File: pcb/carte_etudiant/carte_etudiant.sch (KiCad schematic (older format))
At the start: 3 parts, among them J1 Conn_02x15_Odd_Even, J2 Conn_01x14, U1 NUCLEO64-F103RB

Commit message: * Passage d un connecteur 30 pts à un connecteur 40 pts sur la carte etudiant * Correction sur le fichier de pinout (changement du nom du signal SERVO_PWM en SERVO_VOILE_PWM)
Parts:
- J1: footprint Insa:TE 5530841-2 PCB Edge -> Insa:5-5530843-4-PCB; symbol Connector_Generic:Conn_02x15_Odd_Even -> Connector_Generic:Conn_02x20_Odd_Even
- J2: footprint Connector_PinHeader_2.54mm:PinHeader_1x14_P2.54mm_Vertical -> Connector_PinHeader_2.54mm:PinHeader_1x16_P2.54mm_Vertical; symbol Connector_Generic:Conn_01x14 -> Connector_Generic:Conn_01x16
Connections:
- net labels added: +5V, CAPTEUR_I2C_SCL, CAPTEUR_I2C_SDA, CAPTEUR_SPI_CLK, CAPTEUR_SPI_CS, CAPTEUR_SPI_MISO, CAPTEUR_SPI_MOSI, GIROUETTE_INDEX, GIROUETTE_PHA, GIROUETTE_PHB, PLATEAU_DIRECTION, PLATEAU_PWM, SERVO_VOILE_PWM, TENSION_BATTERIE, XBEE_UART_RX, XBEE_UART_TX
- net labels removed: +3V3
- wire segments 49 -> 65
- no-connect marks 79 -> 83
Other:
- note removed: "Girouette Index"
- note removed: "Girouette PH-A"
- note removed: "Girouette PH-B"
- note removed: "I2C SCL"
- note removed: "I2C SDA"
- note removed: "Moteur Direction"
- note removed: "Moteur PWM"
- note removed: "Servo PWM"
- note removed: "Tension Batterie"
- note removed: "XBEE RX"
- note removed: "XBEE TX"

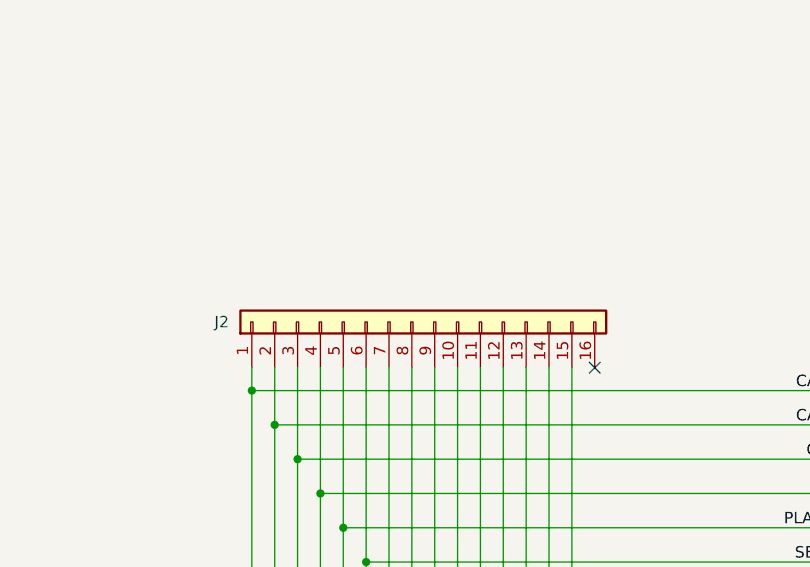
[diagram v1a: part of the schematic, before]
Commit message: modif sur la carte etudiant (changement de coté)
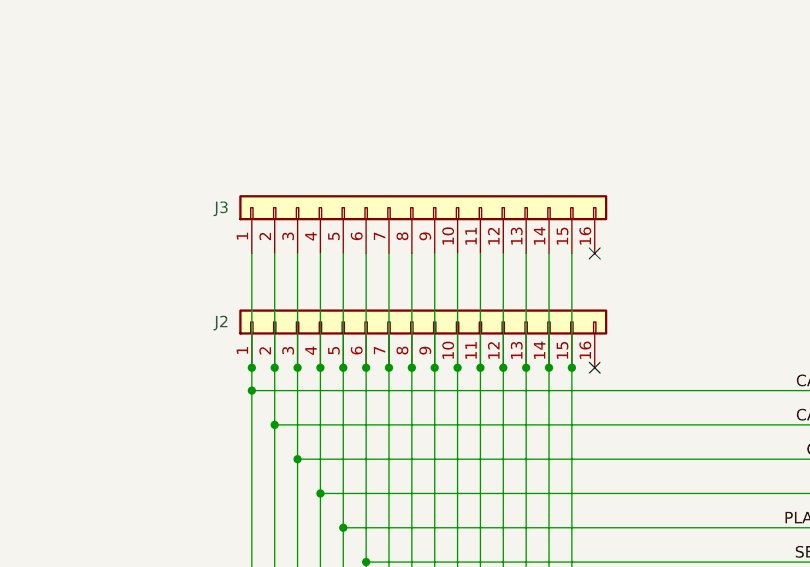
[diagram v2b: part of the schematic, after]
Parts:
- added J3: Conn_01x14, Connector_PinSocket_2.54mm:PinSocket_1x16_P2.54mm_Vertical, symbol Connector_Generic:Conn_01x16
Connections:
- wire segments 65 -> 80
- no-connect marks 83 -> 84
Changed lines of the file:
@@
 	6350 4750 6250 4750
 $Comp
-L power:GND #PWR?
+L power:GND #PWR0101
 U 1 1 5E4A3E36
 P 6250 4750
-F 0 "#PWR?" H 6250 4500 50  0001 C CNN
+F 0 "#PWR0101" H 6250 4500 50  0001 C CNN
 F 1 "GND" H 6255 4577 50  0000 C CNN
 F 2 "" H 6250 4750 50  0001 C CNN
@@
 $EndComp
 $Comp
-L power:GND #PWR?
+L power:GND #PWR0103
 U 1 1 5E4A485B
 P 3700 5350
-F 0 "#PWR?" H 3700 5100 50  0001 C CNN
+F 0 "#PWR0103" H 3700 5100 50  0001 C CNN
 F 1 "GND" H 3705 5177 50  0000 C CNN
 F 2 "" H 3700 5350 50  0001 C CNN
@@
 	3800 1250 3800 950
 $Comp
-L power:+5V #PWR?
+L power:+5V #PWR0104
 U 1 1 5E77E45F
 P 3800 950
-F 0 "#PWR?" H 3800 800 50  0001 C CNN
+F 0 "#PWR0104" H 3800 800 50  0001 C CNN
 F 1 "+5V" H 3815 1123 50  0000 C CNN
 F 2 "" H 3800 950 50  0001 C CNN
@@
 $EndComp
 $Comp
-L power:+5V #PWR?
+L power:+5V #PWR0105
 U 1 1 5E77F67D
 P 10750 1050
-F 0 "#PWR?" H 10750 900 50  0001 C CNN
+F 0 "#PWR0105" H 10750 900 50  0001 C CNN
 F 1 "+5V" H 10765 1223 50  0000 C CNN
 F 2 "" H 10750 1050 50  0001 C CNN
@@
 $EndComp
 $Comp
-L power:+5V #PWR?
+L power:+5V #PWR0106
 U 1 1 5E780E0F
 P 6550 5050
-F 0 "#PWR?" H 6550 4900 50  0001 C CNN
+F 0 "#PWR0106" H 6550 4900 50  0001 C CNN
 F 1 "+5V" H 6565 5223 50  0000 C CNN
 F 2 "" H 6550 5050 50  0001 C CNN
@@
 	1    0    0    -1
 $EndComp
+$Comp
+L Connector_Generic:Conn_01x16 J3
+U 1 1 60081935
+P 7350 1950
+F 0 "J3" V 7350 2750 50  0000 L CNN
+F 1 "Conn_01x14" H 7430 1851 50  0001 L CNN
+F 2 "Connector_PinSocket_2.54mm:PinSocket_1x16_P2.54mm_Vertical" H 7350 1950 50  0001 C CNN
+F 3 "~" H 7350 1950 50  0001 C CNN
+	1    7350 1950
+	0    -1   -1   0
+$EndComp
+Wire Wire Line
+	6650 2650 6650 2150
+Connection ~ 6650 2650
+Wire Wire Line
+	6750 2150 6750 2650
+Connection ~ 6750 2650
+Wire Wire Line
+	6850 2650 6850 2150
+Connection ~ 6850 2650
+Wire Wire Line
+	6950 2150 6950 2650
+Connection ~ 6950 2650
+Wire Wire Line
+	7050 2150 7050 2650
+Connection ~ 7050 2650
+Wire Wire Line
+	7150 2150 7150 2650
+Connection ~ 7150 2650
+Wire Wire Line
+	7250 2150 7250 2650
+Connection ~ 7250 2650
+Wire Wire Line
+	7350 2650 7350 2150
+Connection ~ 7350 2650
+Wire Wire Line
+	7450 2150 7450 2650
+Connection ~ 7450 2650
+Wire Wire Line
+	7550 2650 7550 2150
+Connection ~ 7550 2650
+Wire Wire Line
+	7650 2150 7650 2650
+Connection ~ 7650 2650
+Wire Wire Line
+	7750 2650 7750 2150
+Connection ~ 7750 2650
+Wire Wire Line
+	7850 2150 7850 2650
+Connection ~ 7850 2650
+Wire Wire Line
+	7950 2650 7950 2150
+Connection ~ 7950 2650
+Wire Wire Line
+	8050 2150 8050 2650
+Connection ~ 8050 2650
+NoConn ~ 8150 2150
 $EndSCHEMATC

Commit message: carte terminée
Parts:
- U1: symbol Insa:NUCLEO64-F103RB -> carte_etudiant-rescue:NUCLEO64-F103RB-Insa
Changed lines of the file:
@@
 $EndComp
 $Comp
-L Insa:NUCLEO64-F103RB U1
+L carte_etudiant-rescue:NUCLEO64-F103RB-Insa U1
 U 1 1 5E490880
 P 4000 3250

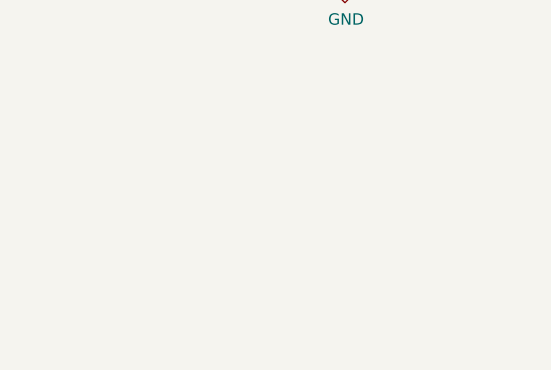
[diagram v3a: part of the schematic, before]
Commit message: rajout de plot de masse + changement taille serigraphie sur carte-etudiant
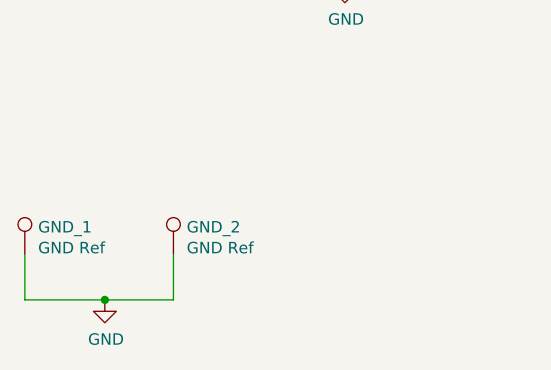
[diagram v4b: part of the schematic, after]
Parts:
- added GND_1, GND_2: GND Ref, Connector_PinHeader_2.54mm:PinHeader_1x01_P2.54mm_Vertical, symbol Connector:TestPoint
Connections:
- net GND: now also GND_1.1, GND_2.1
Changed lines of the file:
@@
 Connection ~ 8050 2650
 NoConn ~ 8150 2150
+$Comp
+L Connector:TestPoint GND_1
+U 1 1 60C8950E
+P 2300 6550
+F 0 "GND_1" H 2358 6668 50  0000 L CNN
+F 1 "GND Ref" H 2358 6577 50  0000 L CNN
+F 2 "Connector_PinHeader_2.54mm:PinHeader_1x01_P2.54mm_Vertical" H 2358 6531 50  0001 L CNN
+F 3 "~" H 2500 6550 50  0001 C CNN
+	1    2300 6550
+	1    0    0    -1
+$EndComp
+$Comp
+L Connector:TestPoint GND_2
+U 1 1 60C89C49
+P 2950 6550
+F 0 "GND_2" H 3008 6668 50  0000 L CNN
+F 1 "GND Ref" H 3008 6577 50  0000 L CNN
+F 2 "Connector_PinHeader_2.54mm:PinHeader_1x01_P2.54mm_Vertical" H 3150 6550 50  0001 C CNN
+F 3 "~" H 3150 6550 50  0001 C CNN
+	1    2950 6550
+	1    0    0    -1
+$EndComp
+$Comp
+L power:GND #PWR0107
+U 1 1 60C93D1F
+P 2650 6750
+F 0 "#PWR0107" H 2650 6500 50  0001 C CNN
+F 1 "GND" H 2655 6577 50  0000 C CNN
+F 2 "" H 2650 6750 50  0001 C CNN
+F 3 "" H 2650 6750 50  0001 C CNN
+	1    2650 6750
+	1    0    0    -1
+$EndComp
+Wire Wire Line
+	2300 6550 2300 6750
+Wire Wire Line
+	2300 6750 2650 6750
+Wire Wire Line
+	2950 6750 2950 6550
+Connection ~ 2650 6750
+Wire Wire Line
+	2650 6750 2950 6750
 $EndSCHEMATC

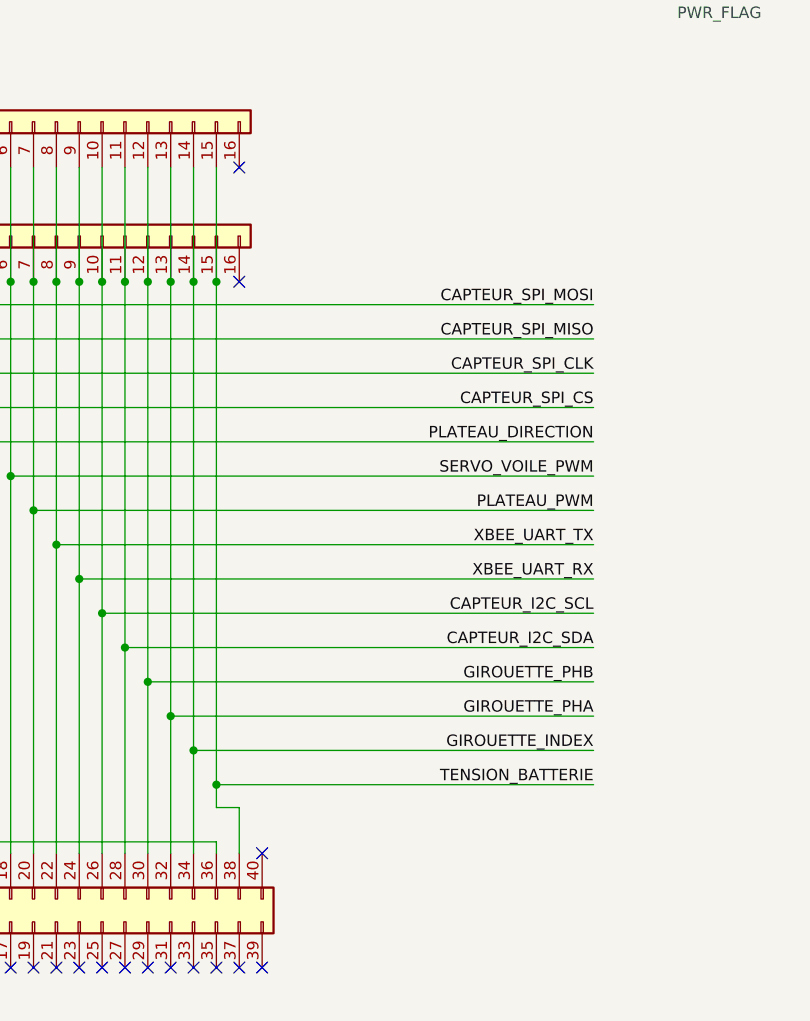
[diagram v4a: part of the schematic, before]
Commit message: Version 1.4 de la carte etudiant, ajout de la ligne SPI_CS2
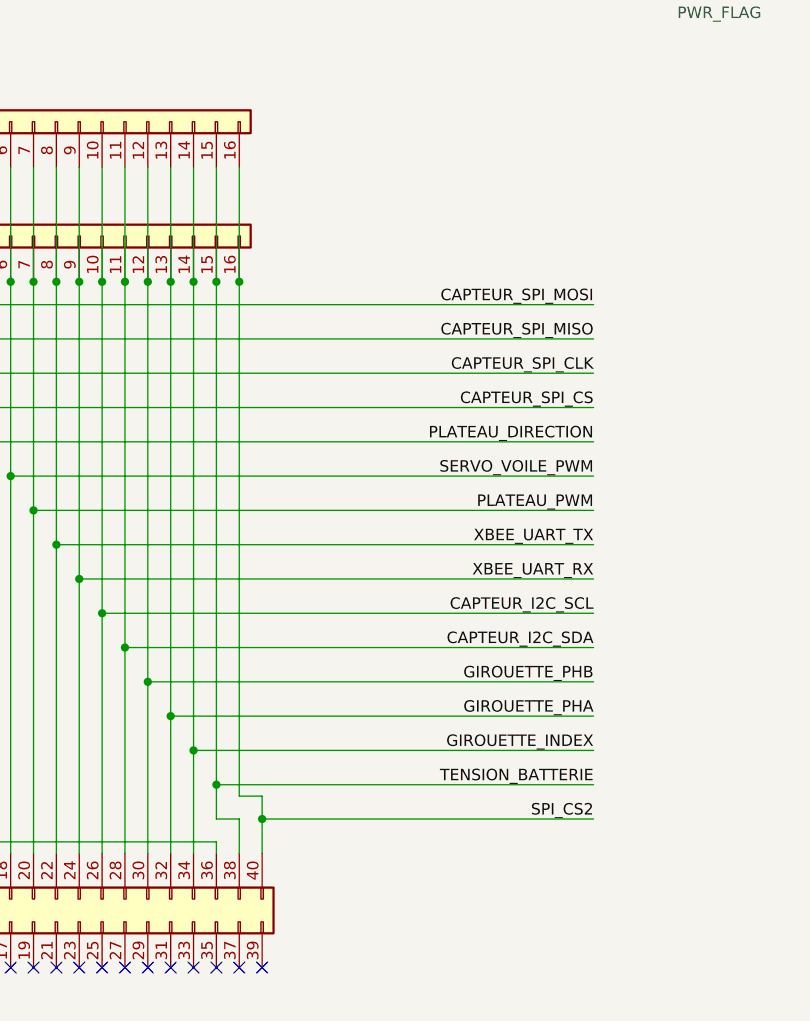
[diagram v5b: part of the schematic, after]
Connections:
- net SPI_CS2: now reaches J1.40 (Pin_40)
- net SPI_CS2: now also J2.16 (Pin_16), J3.16 (Pin_16)
- no-connect marks 84 -> 81
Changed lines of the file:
@@
 Sheet 1 1
 Title "Carte étudiant"
-Date "2020-03-10"
-Rev "1.1"
+Date "2021-06-29"
+Rev "1.4"
 Comp "INSA GEI"
 Comment1 ""
@@
 NoConn ~ 6450 5650
 NoConn ~ 6350 5650
-NoConn ~ 8250 5150
 Wire Wire Line
 	6650 2750 9700 2750
@@
 Wire Wire Line
 	6450 5100 6350 5100
-NoConn ~ 8150 2650
 Wire Wire Line
 	8050 4850 9700 4850
 Wire Wire Line
-	8050 4850 8050 4950
-Wire Wire Line
-	8050 4950 8150 4950
-Wire Wire Line
-	8150 4950 8150 5150
+	8050 5000 8150 5000
 Connection ~ 8050 4850
 Wire Wire Line
@@
 	8050 2150 8050 2650
 Connection ~ 8050 2650
-NoConn ~ 8150 2150
 $Comp
 L Connector:TestPoint GND_1
@@
 Wire Wire Line
 	2650 6750 2950 6750
+Wire Wire Line
+	8150 2150 8150 2650
+Wire Wire Line
+	8150 5000 8150 5150
+Wire Wire Line
+	8050 4850 8050 5000
+Wire Wire Line
+	8250 5150 8250 5000
+Wire Wire Line
+	8250 4900 8150 4900
+Wire Wire Line
+	8150 4900 8150 2650
+Connection ~ 8150 2650
+Wire Wire Line
+	9700 5000 8250 5000
+Connection ~ 8250 5000
+Wire Wire Line
+	8250 5000 8250 4900
+Text Label 9700 5000 2    50   ~ 0
+SPI_CS2
 $EndSCHEMATC

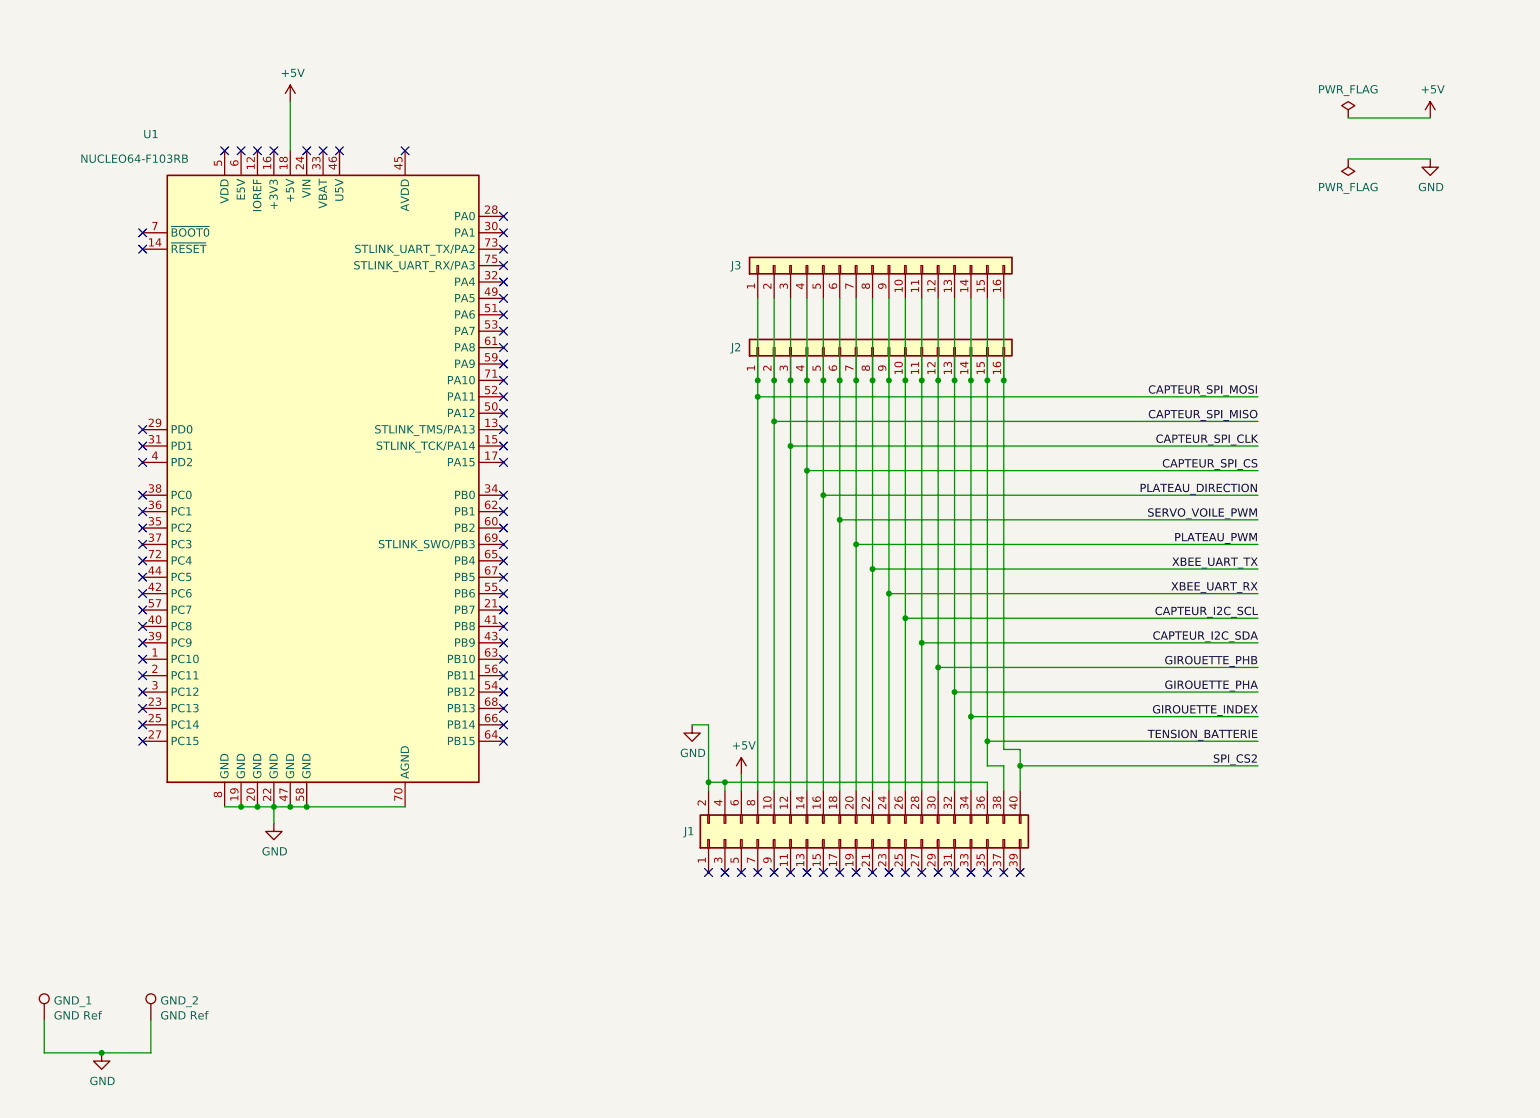
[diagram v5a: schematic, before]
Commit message: Envoi de la rotation toutes les 100 ms + ajout ligne spi_cs2
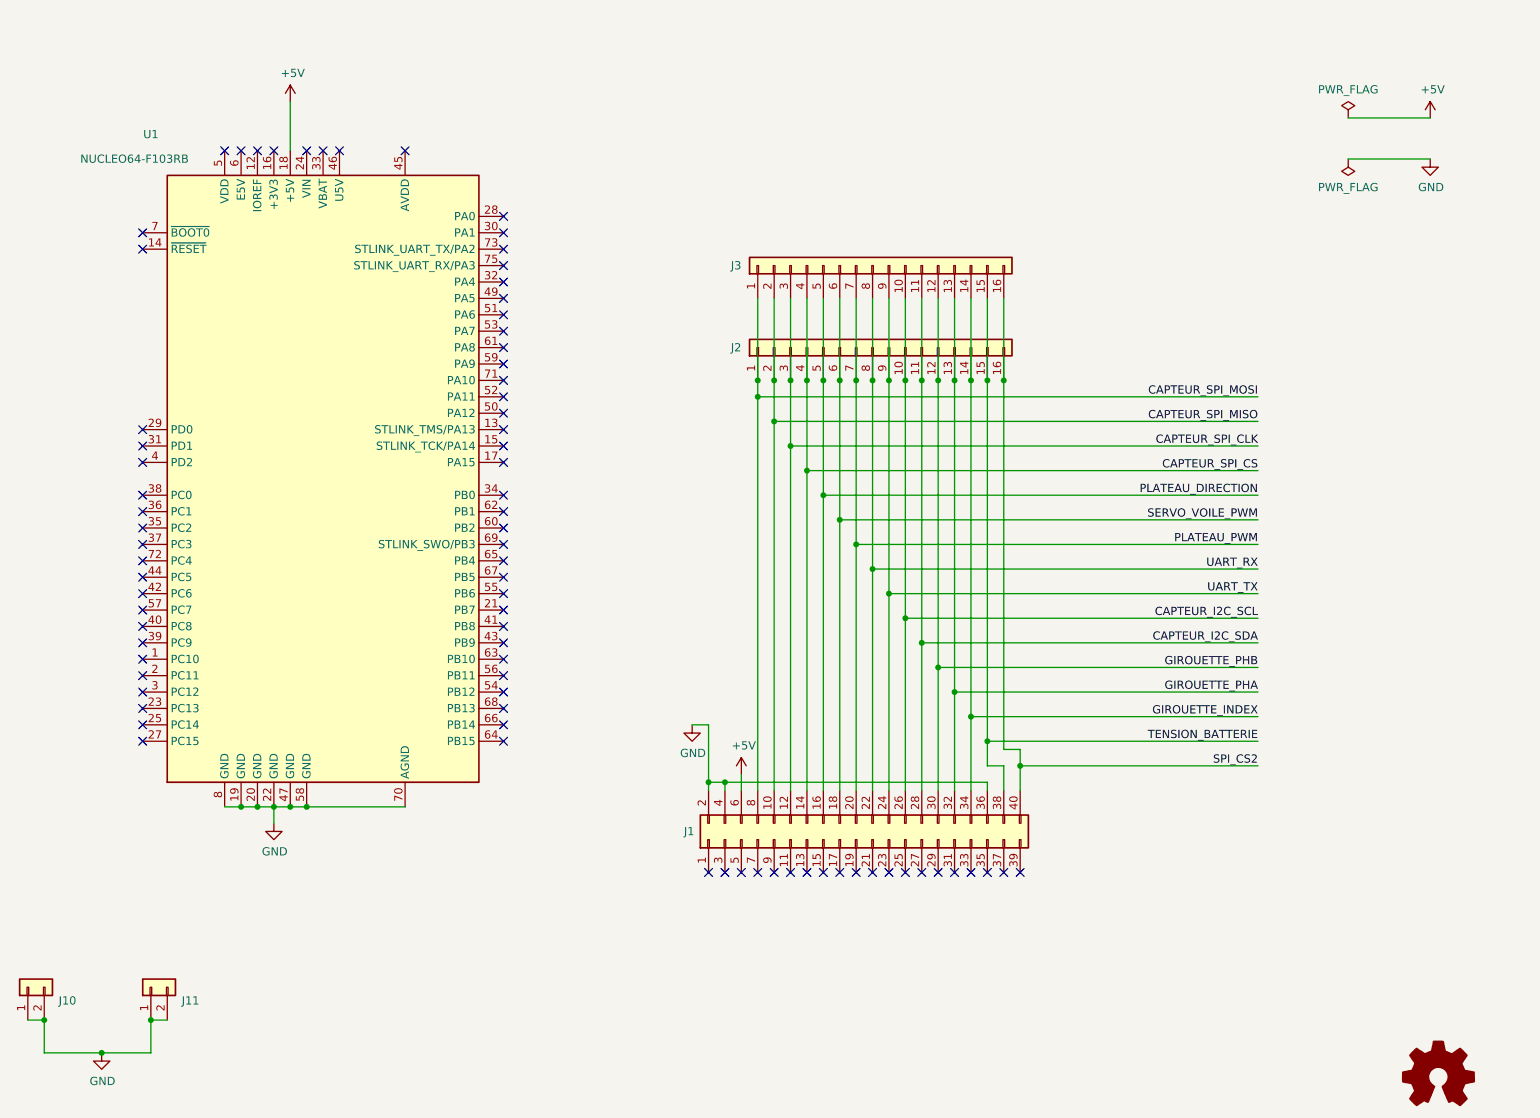
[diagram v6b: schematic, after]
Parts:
- removed GND_1, GND_2: GND Ref, Connector_PinHeader_2.54mm:PinHeader_1x01_P2.54mm_Vertical, symbol Connector:TestPoint
- added J10, J11: Conn_01x02, Connector_PinHeader_2.54mm:PinHeader_1x02_P2.54mm_Vertical, symbol Connector_Generic:Conn_01x02
- added LOGO1: Logo_Open_Hardware_Small, Insa:insa-image, symbol Graphic:Logo_Open_Hardware_Small
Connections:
- net GND: now also J10.1 (Pin_1), J10.2 (Pin_2), J11.1 (Pin_1), J11.2 (Pin_2)
- net XBEE_UART_RX renamed UART_TX
- net XBEE_UART_TX renamed UART_RX
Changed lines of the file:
@@
 PLATEAU_PWM
 Text Label 9700 3800 2    50   ~ 0
-XBEE_UART_TX
+UART_RX
 Text Label 9700 3950 2    50   ~ 0
-XBEE_UART_RX
+UART_TX
 Text Label 9700 4100 2    50   ~ 0
 CAPTEUR_I2C_SCL
@@
 Connection ~ 8050 2650
 $Comp
-L Connector:TestPoint GND_1
-U 1 1 60C8950E
-P 2300 6550
-F 0 "GND_1" H 2358 6668 50  0000 L CNN
-F 1 "GND Ref" H 2358 6577 50  0000 L CNN
-F 2 "Connector_PinHeader_2.54mm:PinHeader_1x01_P2.54mm_Vertical" H 2358 6531 50  0001 L CNN
-F 3 "~" H 2500 6550 50  0001 C CNN
-	1    2300 6550
-	1    0    0    -1
-$EndComp
-$Comp
-L Connector:TestPoint GND_2
-U 1 1 60C89C49
-P 2950 6550
-F 0 "GND_2" H 3008 6668 50  0000 L CNN
-F 1 "GND Ref" H 3008 6577 50  0000 L CNN
-F 2 "Connector_PinHeader_2.54mm:PinHeader_1x01_P2.54mm_Vertical" H 3150 6550 50  0001 C CNN
-F 3 "~" H 3150 6550 50  0001 C CNN
-	1    2950 6550
-	1    0    0    -1
-$EndComp
-$Comp
 L power:GND #PWR0107
 U 1 1 60C93D1F
@@
 Text Label 9700 5000 2    50   ~ 0
 SPI_CS2
+$Comp
+L Graphic:Logo_Open_Hardware_Small LOGO1
+U 1 1 60E31959
+P 10800 6900
+F 0 "LOGO1" H 10800 7175 50  0001 C CNN
+F 1 "Logo_Open_Hardware_Small" H 10800 6675 50  0001 C CNN
+F 2 "Insa:insa-image" H 10800 6900 50  0001 C CNN
+F 3 "~" H 10800 6900 50  0001 C CNN
+	1    10800 6900
+	1    0    0    -1
+$EndComp
+$Comp
+L Connector_Generic:Conn_01x02 J10
+U 1 1 60E869DB
+P 2200 6350
+F 0 "J10" V 2118 6162 50  0000 R CNN
+F 1 "Conn_01x02" V 2073 6162 50  0001 R CNN
+F 2 "Connector_PinHeader_2.54mm:PinHeader_1x02_P2.54mm_Vertical" H 2200 6350 50  0001 C CNN
+F 3 "~" H 2200 6350 50  0001 C CNN
+	1    2200 6350
+	0    -1   -1   0
+$EndComp
+$Comp
+L Connector_Generic:Conn_01x02 J11
+U 1 1 60E86EF8
+P 2950 6350
+F 0 "J11" V 2868 6162 50  0000 R CNN
+F 1 "Conn_01x02" V 2823 6162 50  0001 R CNN
+F 2 "Connector_PinHeader_2.54mm:PinHeader_1x02_P2.54mm_Vertical" H 2950 6350 50  0001 C CNN
+F 3 "~" H 2950 6350 50  0001 C CNN
+	1    2950 6350
+	0    -1   -1   0
+$EndComp
+Wire Wire Line
+	3050 6550 2950 6550
+Connection ~ 2950 6550
+Wire Wire Line
+	2200 6550 2300 6550
+Connection ~ 2300 6550
 $EndSCHEMATC
